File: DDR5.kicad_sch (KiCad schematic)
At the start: 2 parts

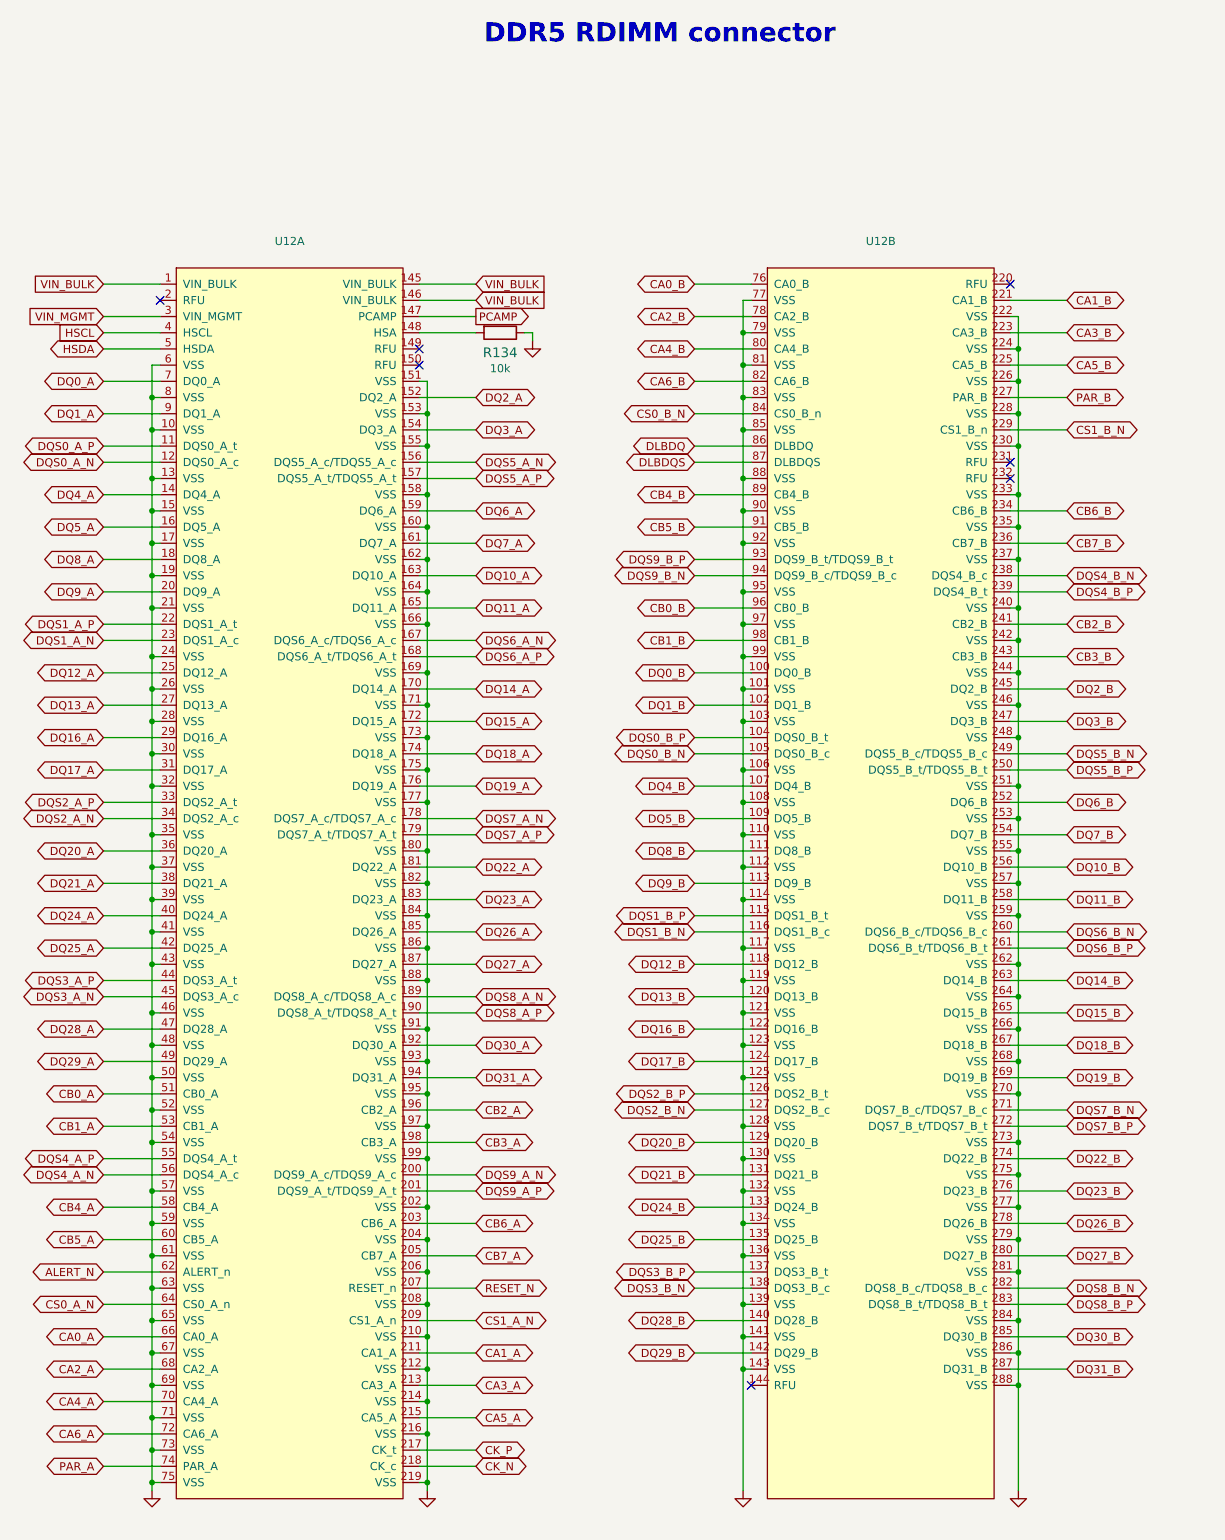
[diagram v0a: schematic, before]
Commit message: Added EN pullup for TPS54561 to avoid disabling by touch
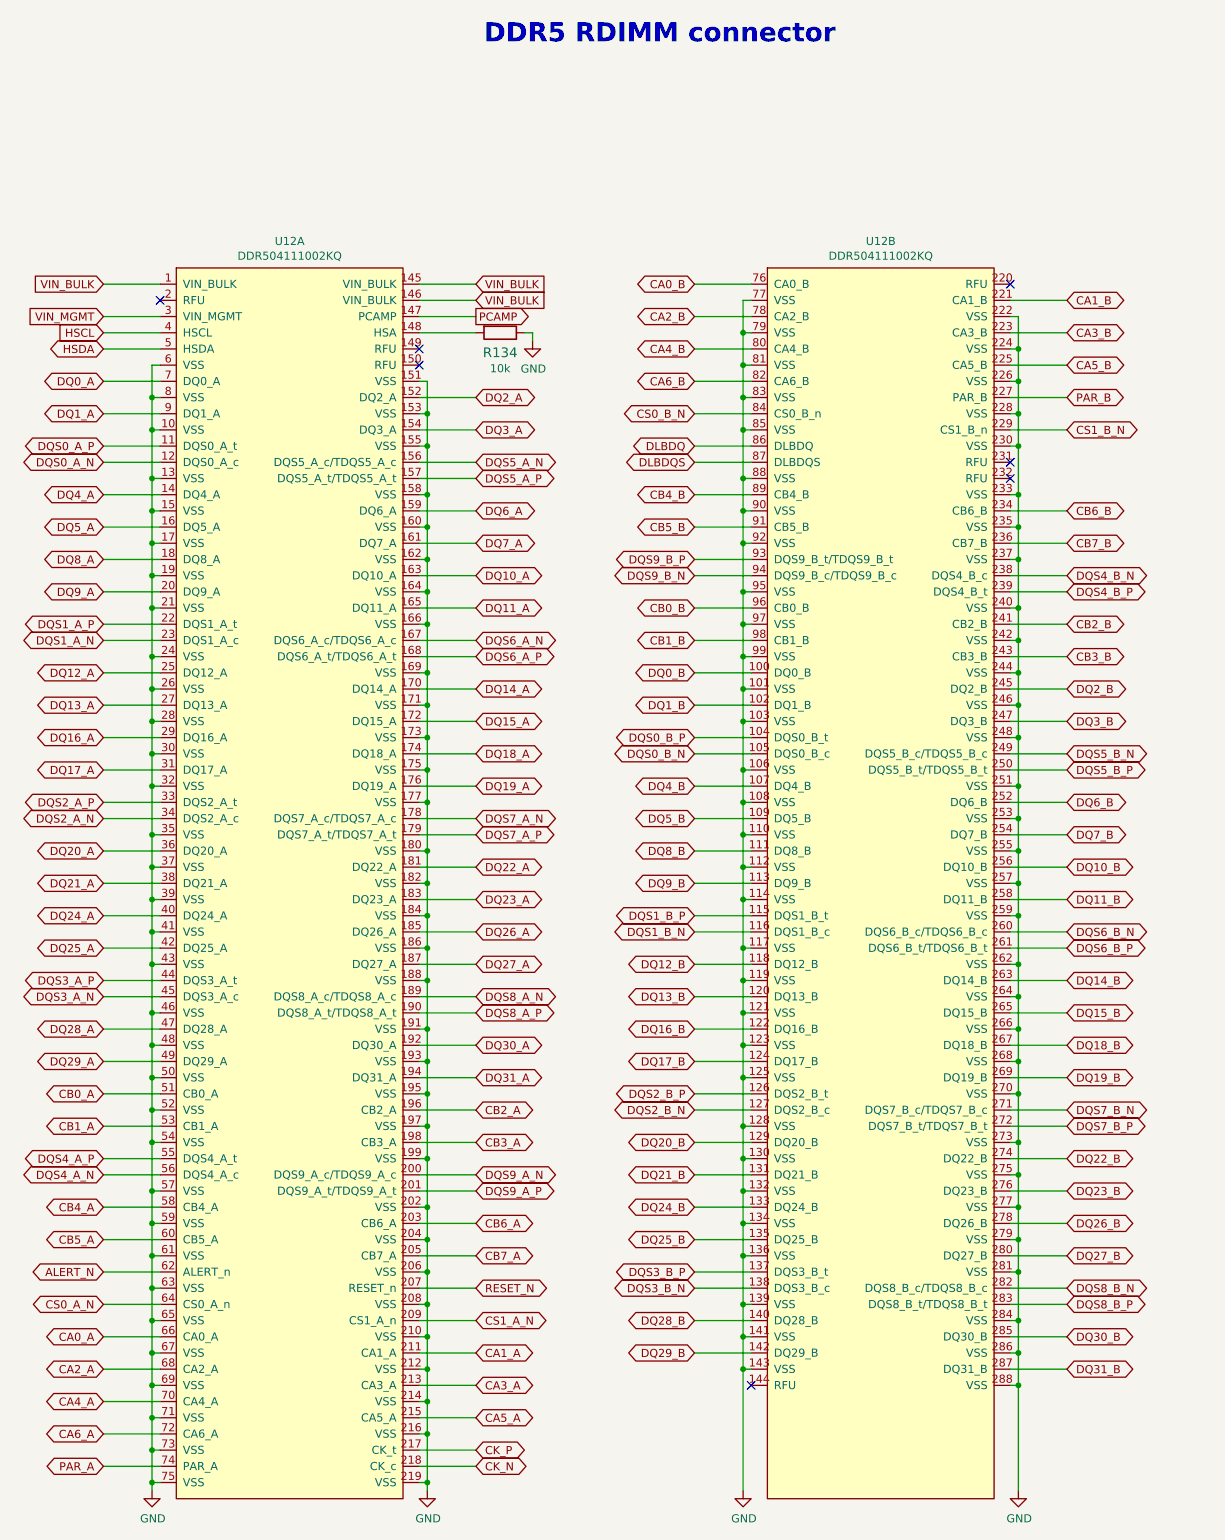
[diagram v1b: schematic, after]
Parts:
- R134: value (none) -> R_10k_0402; footprint (none) -> ddr5-testboard-footprints:0402-res
- U12: value (none) -> DDR504111002KQ; footprint (none) -> ddr5-testboard-footprints:DDR504111002KQ
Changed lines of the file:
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@@
     (in_bom yes) (on_board yes)
     (property "Reference" "U12" (id 0) (at 143.51 56.769 0))
-    (property "Value" "" (id 1) (at 143.51 59.0804 0))
-    (property "Footprint" "" (id 2) (at 126.365 -10.16 0)
+    (property "Value" "DDR504111002KQ" (id 1) (at 143.51 59.0804 0))
+    (property "Footprint" "ddr5-testboard-footprints:DDR504111002KQ" (id 2) (at 126.365 -10.16 0)
       (effects (font (size 1.27 1.27)) hide)
     )
@@
     (in_bom yes) (on_board yes)
     (property "Reference" "U12" (id 0) (at 236.22 56.769 0))
-    (property "Value" "" (id 1) (at 236.22 59.0804 0))
-    (property "Footprint" "" (id 2) (at 219.075 -10.16 0)
+    (property "Value" "DDR504111002KQ" (id 1) (at 236.22 59.0804 0))
+    (property "Footprint" "ddr5-testboard-footprints:DDR504111002KQ" (id 2) (at 219.075 -10.16 0)
       (effects (font (size 1.27 1.27)) hide)
     )
@@
   (symbol (lib_id "ddr5-testboard:GND") (at 165.1 252.73 0) (unit 1)
     (in_bom yes) (on_board yes)
-    (property "Reference" "#PWR?" (id 0) (at 165.1 259.08 0)
-      (effects (font (size 1.27 1.27)) hide)
-    )
-    (property "Value" "" (id 1) (at 165.227 257.1242 0))
+    (property "Reference" "#PWR0194" (id 0) (at 165.1 259.08 0)
+      (effects (font (size 1.27 1.27)) hide)
+    )
+    (property "Value" "GND" (id 1) (at 165.227 257.1242 0))
     (property "Footprint" "" (id 2) (at 165.1 252.73 0)
       (effects (font (size 1.27 1.27)) hide)
@@
   (symbol (lib_id "ddr5-testboard:GND") (at 121.92 252.73 0) (unit 1)
     (in_bom yes) (on_board yes)
-    (property "Reference" "#PWR?" (id 0) (at 121.92 259.08 0)
-      (effects (font (size 1.27 1.27)) hide)
-    )
-    (property "Value" "" (id 1) (at 122.047 257.1242 0))
+    (property "Reference" "#PWR0193" (id 0) (at 121.92 259.08 0)
+      (effects (font (size 1.27 1.27)) hide)
+    )
+    (property "Value" "GND" (id 1) (at 122.047 257.1242 0))
     (property "Footprint" "" (id 2) (at 121.92 252.73 0)
       (effects (font (size 1.27 1.27)) hide)
@@
   (symbol (lib_id "ddr5-testboard:GND") (at 257.81 252.73 0) (unit 1)
     (in_bom yes) (on_board yes)
-    (property "Reference" "#PWR?" (id 0) (at 257.81 259.08 0)
-      (effects (font (size 1.27 1.27)) hide)
-    )
-    (property "Value" "" (id 1) (at 257.937 257.1242 0))
+    (property "Reference" "#PWR0196" (id 0) (at 257.81 259.08 0)
+      (effects (font (size 1.27 1.27)) hide)
+    )
+    (property "Value" "GND" (id 1) (at 257.937 257.1242 0))
     (property "Footprint" "" (id 2) (at 257.81 252.73 0)
       (effects (font (size 1.27 1.27)) hide)
@@
   (symbol (lib_id "ddr5-testboard:GND") (at 214.63 252.73 0) (unit 1)
     (in_bom yes) (on_board yes)
-    (property "Reference" "#PWR?" (id 0) (at 214.63 259.08 0)
-      (effects (font (size 1.27 1.27)) hide)
-    )
-    (property "Value" "" (id 1) (at 214.757 257.1242 0))
+    (property "Reference" "#PWR0195" (id 0) (at 214.63 259.08 0)
+      (effects (font (size 1.27 1.27)) hide)
+    )
+    (property "Value" "GND" (id 1) (at 214.757 257.1242 0))
     (property "Footprint" "" (id 2) (at 214.63 252.73 0)
       (effects (font (size 1.27 1.27)) hide)
@@
       (effects (font (size 1.524 1.524)))
     )
-    (property "Value" "" (id 1) (at 176.53 67.31 0)
+    (property "Value" "R_10k_0402" (id 1) (at 176.53 67.31 0)
       (effects (font (size 1.524 1.524)) hide)
     )
-    (property "Footprint" "" (id 2) (at 171.45 76.2 0)
+    (property "Footprint" "ddr5-testboard-footprints:0402-res" (id 2) (at 171.45 76.2 0)
       (effects (font (size 1.524 1.524)) (justify left) hide)
     )
@@
   (symbol (lib_id "ddr5-testboard:GND") (at 181.61 72.39 0) (unit 1)
     (in_bom yes) (on_board yes)
-    (property "Reference" "#PWR?" (id 0) (at 181.61 78.74 0)
-      (effects (font (size 1.27 1.27)) hide)
-    )
-    (property "Value" "" (id 1) (at 181.737 76.7842 0))
+    (property "Reference" "#PWR0217" (id 0) (at 181.61 78.74 0)
+      (effects (font (size 1.27 1.27)) hide)
+    )
+    (property "Value" "GND" (id 1) (at 181.737 76.7842 0))
     (property "Footprint" "" (id 2) (at 181.61 72.39 0)
       (effects (font (size 1.27 1.27)) hide)

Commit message: Update naming convention
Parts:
- R134: footprint ddr5-testboard-footprints:0402-res -> data-center-rdimm-ddr5-tester-footprints:0402-res; symbol ddr5-testboard:R_10k_0402 -> data-center-rdimm-ddr5-tester:R_10k_0402
- U12: footprint ddr5-testboard-footprints:DDR504111002KQ -> data-center-rdimm-ddr5-tester-footprints:DDR504111002KQ; symbol ddr5-testboard:DDR504111002KQ -> data-center-rdimm-ddr5-tester:DDR504111002KQ
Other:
- title: DDR5 Tester -> Data Center RDIMM DDR5 Tester
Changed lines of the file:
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@@
   (paper "A3")
   (title_block
-    (title "DDR5 Tester")
+    (title "Data Center RDIMM DDR5 Tester")
     (date "2022-03-08")
     (rev "1.0.0")
@@
     )
   )
-  (symbol (lib_id "ddr5-testboard:DDR504111002KQ") (at 143.51 160.02 0) (unit 1)
+  (symbol (lib_id "data-center-rdimm-ddr5-tester:DDR504111002KQ") (at 143.51 160.02 0) (unit 1)
     (in_bom yes) (on_board yes)
     (property "Reference" "U12" (id 0) (at 143.51 56.769 0))
     (property "Value" "DDR504111002KQ" (id 1) (at 143.51 59.0804 0))
-    (property "Footprint" "ddr5-testboard-footprints:DDR504111002KQ" (id 2) (at 126.365 -10.16 0)
+    (property "Footprint" "data-center-rdimm-ddr5-tester-footprints:DDR504111002KQ" (id 2) (at 126.365 -10.16 0)
       (effects (font (size 1.27 1.27)) hide)
     )
@@
     (pin "99")
   )
-  (symbol (lib_id "ddr5-testboard:DDR504111002KQ") (at 236.22 160.02 0) (unit 2)
+  (symbol (lib_id "data-center-rdimm-ddr5-tester:DDR504111002KQ") (at 236.22 160.02 0) (unit 2)
     (in_bom yes) (on_board yes)
     (property "Reference" "U12" (id 0) (at 236.22 56.769 0))
     (property "Value" "DDR504111002KQ" (id 1) (at 236.22 59.0804 0))
-    (property "Footprint" "ddr5-testboard-footprints:DDR504111002KQ" (id 2) (at 219.075 -10.16 0)
+    (property "Footprint" "data-center-rdimm-ddr5-tester-footprints:DDR504111002KQ" (id 2) (at 219.075 -10.16 0)
       (effects (font (size 1.27 1.27)) hide)
     )
@@
     (pin "99")
   )
-  (symbol (lib_id "ddr5-testboard:GND") (at 165.1 252.73 0) (unit 1)
+  (symbol (lib_id "data-center-rdimm-ddr5-tester:GND") (at 165.1 252.73 0) (unit 1)
     (in_bom yes) (on_board yes)
     (property "Reference" "#PWR0194" (id 0) (at 165.1 259.08 0)
@@
     (pin "1")
   )
-  (symbol (lib_id "ddr5-testboard:GND") (at 121.92 252.73 0) (unit 1)
+  (symbol (lib_id "data-center-rdimm-ddr5-tester:GND") (at 121.92 252.73 0) (unit 1)
     (in_bom yes) (on_board yes)
     (property "Reference" "#PWR0193" (id 0) (at 121.92 259.08 0)
@@
     (pin "1")
   )
-  (symbol (lib_id "ddr5-testboard:GND") (at 257.81 252.73 0) (unit 1)
+  (symbol (lib_id "data-center-rdimm-ddr5-tester:GND") (at 257.81 252.73 0) (unit 1)
     (in_bom yes) (on_board yes)
     (property "Reference" "#PWR0196" (id 0) (at 257.81 259.08 0)
@@
     (pin "1")
   )
-  (symbol (lib_id "ddr5-testboard:GND") (at 214.63 252.73 0) (unit 1)
+  (symbol (lib_id "data-center-rdimm-ddr5-tester:GND") (at 214.63 252.73 0) (unit 1)
     (in_bom yes) (on_board yes)
     (property "Reference" "#PWR0195" (id 0) (at 214.63 259.08 0)
@@
     (pin "1")
   )
-  (symbol (lib_id "ddr5-testboard:R_10k_0402") (at 176.53 71.12 180) (unit 1)
+  (symbol (lib_id "data-center-rdimm-ddr5-tester:R_10k_0402") (at 176.53 71.12 180) (unit 1)
     (in_bom yes) (on_board yes)
     (property "Reference" "R134" (id 0) (at 176.53 74.2442 0)
@@
       (effects (font (size 1.524 1.524)) hide)
     )
-    (property "Footprint" "ddr5-testboard-footprints:0402-res" (id 2) (at 171.45 76.2 0)
+    (property "Footprint" "data-center-rdimm-ddr5-tester-footprints:0402-res" (id 2) (at 171.45 76.2 0)
       (effects (font (size 1.524 1.524)) (justify left) hide)
     )
@@
     (pin "2")
   )
-  (symbol (lib_id "ddr5-testboard:GND") (at 181.61 72.39 0) (unit 1)
+  (symbol (lib_id "data-center-rdimm-ddr5-tester:GND") (at 181.61 72.39 0) (unit 1)
     (in_bom yes) (on_board yes)
     (property "Reference" "#PWR0217" (id 0) (at 181.61 78.74 0)
